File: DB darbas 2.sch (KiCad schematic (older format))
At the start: 20 parts, among them J1 XLR3_Ground, J3 XLR3_Ground, SW6 SW_DPST_x2, U1 Arduino_UNO_R2

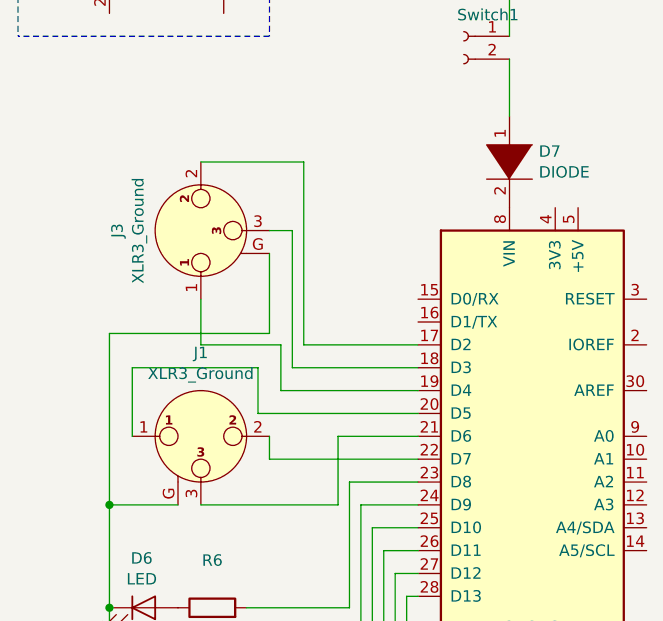
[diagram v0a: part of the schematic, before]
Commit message: DMX laidų testeris REV 1.2
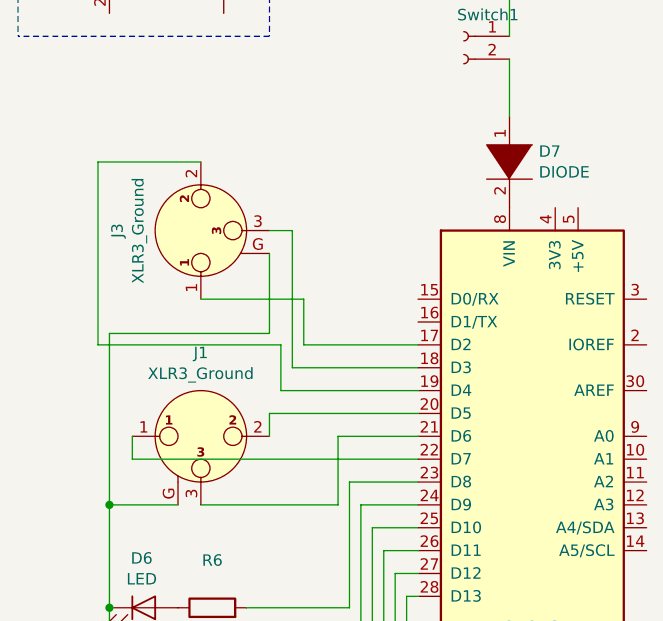
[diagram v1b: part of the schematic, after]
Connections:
- net at U1.17 (D2): now also J3.1; no longer J3.2
- net at U1.19 (D4): now also J3.2; no longer J3.1
- net at U1.20 (D5): now also J1.2; no longer J1.1
- net at U1.22 (D7): now also J1.1; no longer J1.2
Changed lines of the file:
@@
 Connection ~ 3700 5300
-Wire Wire Line
-	5050 2700 4350 2700
-Wire Wire Line
-	4350 2700 4350 2500
 Wire Wire Line
 	5050 2800 4700 2800
 Wire Wire Line
 	4700 2800 4700 3100
-Wire Wire Line
-	5050 2900 4400 2900
-Wire Wire Line
-	4400 2900 4400 2800
 Wire Wire Line
 	5650 4300 5550 4300
@@
 Wire Wire Line
 	5550 3900 5550 4300
-Wire Wire Line
-	4350 2500 3800 2500
-Wire Wire Line
-	3800 2500 3800 2800
 Wire Wire Line
 	4700 3100 4100 3100
@@
 	3700 3550 3700 3900
 Wire Wire Line
-	4100 1600 4550 1600
-Wire Wire Line
 	5550 5400 5550 5500
 Wire Wire Line
@@
 	3700 2350 3700 3100
 Connection ~ 3700 3100
-Wire Wire Line
-	4100 2200 4100 2400
-Wire Wire Line
-	4100 2400 4450 2400
 $Comp
 L pspice:DIODE D7
@@
 $EndComp
 Wire Wire Line
-	4550 1600 4550 2400
-Wire Wire Line
 	5450 1400 5450 1150
 Text Notes 4450 600  0    50   ~ 0
 Nemontuojama į PCB\n
+Wire Wire Line
+	3650 2400 3650 1600
+Wire Wire Line
+	3650 1600 4100 1600
+Wire Wire Line
+	3650 2400 4450 2400
+Wire Wire Line
+	4550 2400 4550 2200
+Wire Wire Line
+	4550 2200 4100 2200
+Wire Wire Line
+	5050 2700 4400 2700
+Wire Wire Line
+	4400 2700 4400 2800
+Wire Wire Line
+	5050 2900 3800 2900
+Wire Wire Line
+	3800 2900 3800 2800
 $EndSCHEMATC

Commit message: Ver1.3
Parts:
- removed Switch1: Conn_01x02_Female, Connector_PinHeader_2.54mm:PinHeader_1x02_P2.54mm_Horizontal, symbol Connector:Conn_01x02_Female
- removed VCC1: Connector, Connector_PinHeader_2.54mm:PinHeader_1x02_P2.54mm_Horizontal, symbol Connector:Conn_01x02_Female
- renumbered DC_9V1 to B1, J3 to J1, J1 to J2, SW6 to SW1
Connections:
- net GND: now also B1.2 (-)
- net at B1.1 (+): now also SW1.2 (B)
- net at SW1.1 (A): now also D7.1 (K)
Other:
- note removed: "Nemontuojama į PCB\n"
- moved on the sheet: B1, J1, J2, SW1A
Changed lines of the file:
@@
 U 1 1 5BE0B862
 P 3850 4600
-F 0 "D3" H 3841 4816 50  0000 C CNN
-F 1 "LED" H 3841 4725 50  0000 C CNN
+F 0 "D3" H 3850 5060 50  0000 C CNN
+F 1 "LED" H 3841 4725 50  0001 C CNN
 F 2 "LED_SMD:LED_0603_1608Metric_Pad1.05x0.95mm_HandSolder" H 3850 4600 50  0001 C CNN
 F 3 "~" H 3850 4600 50  0001 C CNN
@@
 U 1 1 5BE0B8D5
 P 4150 4600
-F 0 "R3" V 4357 4600 50  0000 C CNN
+F 0 "R3" V 4610 4600 50  0000 C CNN
 F 1 "300" V 4250 4550 50  0001 C CNN
 F 2 "Resistor_SMD:R_0603_1608Metric_Pad1.05x0.95mm_HandSolder" V 4080 4600 50  0001 C CNN
@@
 $EndComp
 $Comp
-L Device:Battery DC_9V1
+L Device:Battery B1
 U 1 1 5BE0F56A
-P 4200 750
-F 0 "DC_9V1" V 4445 750 50  0000 C CNN
-F 1 "Battery" V 4354 750 50  0001 C CNN
-F 2 "" V 4200 810 50  0001 C CNN
-F 3 "~" V 4200 810 50  0001 C CNN
-	1    4200 750
-	-1   0    0    1
-$EndComp
-Wire Wire Line
-	7100 800  7100 4300
+P 6750 1400
+F 0 "B1" V 6600 1400 50  0000 C CNN
+F 1 "Battery" V 6904 1400 50  0001 C CNN
+F 2 "" V 6750 1460 50  0001 C CNN
+F 3 "~" V 6750 1460 50  0001 C CNN
+	1    6750 1400
+	0    -1   -1   0
+$EndComp
 Wire Wire Line
 	7100 4300 5650 4300
@@
 	5650 4300 5650 3900
 $Comp
-L Switch:SW_DPST_x2 SW6
+L Switch:SW_DPST_x2 SW1
 U 1 1 5BE115DF
-P 3700 750
-F 0 "SW6" V 3746 662 50  0000 R CNN
-F 1 "SW_DPST_x2" V 3655 662 50  0001 R CNN
-F 2 "" H 3700 750 50  0001 C CNN
-F 3 "" H 3700 750 50  0001 C CNN
-	1    3700 750
-	0    1    1    0
+P 6000 1400
+F 0 "SW1" H 6100 1300 50  0000 R CNN
+F 1 "SW_DPST_x2" V 5955 1312 50  0001 R CNN
+F 2 "" H 6000 1400 50  0001 C CNN
+F 3 "" H 6000 1400 50  0001 C CNN
+	1    6000 1400
+	1    0    0    -1
 $EndComp
 $Comp
@@
 U 1 1 5BE11DF9
 P 3850 4250
-F 0 "D4" H 3841 4466 50  0000 C CNN
-F 1 "LED" H 3841 4375 50  0000 C CNN
+F 0 "D4" H 3850 4000 50  0000 C CNN
+F 1 "LED" H 3841 4375 50  0001 C CNN
 F 2 "LED_SMD:LED_0603_1608Metric_Pad1.05x0.95mm_HandSolder" H 3850 4250 50  0001 C CNN
 F 3 "~" H 3850 4250 50  0001 C CNN
@@
 U 1 1 5BE11DFF
 P 4150 4250
-F 0 "R4" V 4350 4250 50  0000 C CNN
+F 0 "R4" V 3900 4250 50  0000 C CNN
 F 1 "300" V 4250 4200 50  0001 C CNN
 F 2 "Resistor_SMD:R_0603_1608Metric_Pad1.05x0.95mm_HandSolder" V 4080 4250 50  0001 C CNN
@@
 U 1 1 5BE11FA5
 P 3850 5300
-F 0 "D1" H 3841 5516 50  0000 C CNN
-F 1 "LED" H 3841 5425 50  0000 C CNN
+F 0 "D1" H 3860 7150 50  0000 C CNN
+F 1 "LED" H 3841 5425 50  0001 C CNN
 F 2 "LED_SMD:LED_0603_1608Metric_Pad1.05x0.95mm_HandSolder" H 3850 5300 50  0001 C CNN
 F 3 "~" H 3850 5300 50  0001 C CNN
@@
 U 1 1 5BE11FAB
 P 4150 5300
-F 0 "R1" V 3950 5300 50  0000 C TNN
+F 0 "R1" V 2270 5300 50  0000 C TNN
 F 1 "300" V 4050 5350 50  0001 C CNN
 F 2 "Resistor_SMD:R_0603_1608Metric_Pad1.05x0.95mm_HandSolder" V 4080 5300 50  0001 C CNN
@@
 U 1 1 5BE11FB1
 P 3850 4950
-F 0 "D2" H 3841 5166 50  0000 C CNN
-F 1 "LED" H 3841 5075 50  0000 C CNN
+F 0 "D2" H 3850 6100 50  0000 C CNN
+F 1 "LED" H 3841 5075 50  0001 C CNN
 F 2 "LED_SMD:LED_0603_1608Metric_Pad1.05x0.95mm_HandSolder" H 3850 4950 50  0001 C CNN
 F 3 "~" H 3850 4950 50  0001 C CNN
@@
 U 1 1 5BE11FB7
 P 4150 4950
-F 0 "R2" V 4357 4950 50  0000 C CNN
+F 0 "R2" V 5300 4950 50  0000 C CNN
 F 1 "300" V 4250 4900 50  0001 C CNN
 F 2 "Resistor_SMD:R_0603_1608Metric_Pad1.05x0.95mm_HandSolder" V 4080 4950 50  0001 C CNN
@@
 U 1 1 5BE120E5
 P 3850 3900
-F 0 "D5" H 3841 4116 50  0000 C CNN
-F 1 "LED" H 3841 4025 50  0000 C CNN
+F 0 "D5" H 3840 2950 50  0000 C CNN
+F 1 "LED" H 3841 4025 50  0001 C CNN
 F 2 "LED_SMD:LED_0603_1608Metric_Pad1.05x0.95mm_HandSolder" H 3850 3900 50  0001 C CNN
 F 3 "~" H 3850 3900 50  0001 C CNN
@@
 U 1 1 5BE120EB
 P 4150 3900
-F 0 "R5" V 4357 3900 50  0000 C CNN
+F 0 "R5" V 3200 3910 50  0000 C CNN
 F 1 "300" V 4250 3850 50  0001 C CNN
 F 2 "Resistor_SMD:R_0603_1608Metric_Pad1.05x0.95mm_HandSolder" V 4080 3900 50  0001 C CNN
@@
 U 1 1 5BE120F1
 P 3850 3550
-F 0 "D6" H 3841 3766 50  0000 C CNN
-F 1 "LED" H 3841 3675 50  0000 C CNN
+F 0 "D6" H 3850 1900 50  0000 C CNN
+F 1 "LED" H 3841 3675 50  0001 C CNN
 F 2 "LED_SMD:LED_0603_1608Metric_Pad1.05x0.95mm_HandSolder" H 3850 3550 50  0001 C CNN
 F 3 "~" H 3850 3550 50  0001 C CNN
@@
 U 1 1 5BE120F7
 P 4150 3550
-F 0 "R6" V 4357 3550 50  0000 C CNN
+F 0 "R6" V 2500 3570 50  0000 C CNN
 F 1 "300" V 4250 3500 50  0001 C CNN
 F 2 "Resistor_SMD:R_0603_1608Metric_Pad1.05x0.95mm_HandSolder" V 4080 3550 50  0001 C CNN
@@
 	0    -1   -1   0
 $EndComp
-$Comp
-L Connector:Conn_01x02_Female VCC1
-U 1 1 5BE12452
-P 5600 600
-F 0 "VCC1" V 5540 412 50  0000 R CNN
-F 1 "Connector" V 5449 412 50  0001 R CNN
-F 2 "Connector_PinHeader_2.54mm:PinHeader_1x02_P2.54mm_Horizontal" H 5600 600 50  0001 C CNN
-F 3 "~" H 5600 600 50  0001 C CNN
-	1    5600 600
-	0    -1   -1   0
-$EndComp
-$Comp
-L Connector:Conn_01x02_Female Switch1
-U 1 1 5BE124E0
-P 5250 1050
-F 0 "Switch1" H 5144 1143 50  0000 C CNN
-F 1 "Conn_01x02_Female" H 5144 1144 50  0001 C CNN
-F 2 "Connector_PinHeader_2.54mm:PinHeader_1x02_P2.54mm_Horizontal" H 5250 1050 50  0001 C CNN
-F 3 "~" H 5250 1050 50  0001 C CNN
-	1    5250 1050
-	-1   0    0    -1
-$EndComp
-Wire Wire Line
-	5450 800  5450 1050
-Wire Wire Line
-	5450 800  5600 800
-Wire Wire Line
-	5700 800  6300 800
 Wire Wire Line
 	3700 5300 3700 4950
@@
 	4750 3000 5050 3000
 Wire Wire Line
-	4450 2400 4450 2600
-Wire Wire Line
 	4450 2600 5050 2600
-Wire Wire Line
-	4500 1900 4500 2500
-Wire Wire Line
-	4500 2500 5050 2500
-Wire Wire Line
-	4550 2400 5050 2400
 Wire Wire Line
 	5550 5400 3700 5400
@@
 	3700 5400 3700 5300
 Connection ~ 3700 5300
-Wire Wire Line
-	5050 2800 4700 2800
-Wire Wire Line
-	4700 2800 4700 3100
 Wire Wire Line
 	5650 4300 5550 4300
@@
 Wire Wire Line
 	5550 4300 5550 5400
-Wire Notes Line
-	3300 500  4400 500
-Wire Notes Line
-	4400 500  4400 1050
-Wire Notes Line
-	4400 1050 3300 1050
-Wire Notes Line
-	3300 500  3300 1050
 Wire Wire Line
 	5550 3900 5550 4300
-Wire Wire Line
-	4700 3100 4100 3100
-Text Label 6000 800  0    50   ~ 0
-vcc
 $Comp
 L power:GND #PWR0101
@@
 Connection ~ 5550 5400
 $Comp
-L power:VCC #PWR0102
-U 1 1 5BFC947E
-P 6300 800
-F 0 "#PWR0102" H 6300 650 50  0001 C CNN
-F 1 "VCC" H 6317 973 50  0000 C CNN
-F 2 "" H 6300 800 50  0001 C CNN
-F 3 "" H 6300 800 50  0001 C CNN
-	1    6300 800
-	1    0    0    -1
-$EndComp
-Connection ~ 6300 800
-Wire Wire Line
-	6300 800  7100 800
-$Comp
-L Connector:XLR3_Ground J3
+L Connector:XLR3_Ground J1
 U 1 1 5BFCA7B8
-P 4100 1900
-F 0 "J3" H 4100 2265 50  0000 C CNN
-F 1 "XLR3_Ground" H 4100 2174 50  0000 C CNN
-F 2 "XLR_mano:XLR_footprint" H 4100 1900 50  0001 C CNN
-F 3 " ~" H 4100 1900 50  0001 C CNN
-	1    4100 1900
-	0    -1   -1   0
-$EndComp
-$Comp
-L Connector:XLR3_Ground J1
-U 1 1 5BFD097B
-P 4100 2800
-F 0 "J1" H 4100 3165 50  0000 C CNN
-F 1 "XLR3_Ground" H 4100 3074 50  0000 C CNN
-F 2 "XLR_mano:XLR_footprint" H 4100 2800 50  0001 C CNN
-F 3 " ~" H 4100 2800 50  0001 C CNN
-	1    4100 2800
-	1    0    0    -1
-$EndComp
-Wire Wire Line
-	4000 3100 3700 3100
-Wire Wire Line
-	3700 3100 3700 3550
+P 4100 2000
+F 0 "J1" V 4100 2250 50  0000 C CNN
+F 1 "XLR3_Ground" H 4100 2274 50  0001 C CNN
+F 2 "XLR_mano:XLR_footprint" H 4100 2000 50  0001 C CNN
+F 3 " ~" H 4100 2000 50  0001 C CNN
+	1    4100 2000
+	0    1    1    0
+$EndComp
 Connection ~ 3700 3550
 Wire Wire Line
@@
 Wire Wire Line
 	5550 5400 5550 5500
-Wire Wire Line
-	4400 1900 4500 1900
-Wire Wire Line
-	4400 2000 4400 2350
-Wire Wire Line
-	4400 2350 3700 2350
-Wire Wire Line
-	3700 2350 3700 3100
-Connection ~ 3700 3100
 $Comp
 L pspice:DIODE D7
 U 1 1 5BFC56E1
 P 5450 1600
-F 0 "D7" V 5404 1728 50  0000 L CNN
-F 1 "DIODE" V 5495 1728 50  0000 L CNN
+F 0 "D7" V 5450 1750 50  0000 L CNN
+F 1 "DIODE" V 5495 1728 50  0001 L CNN
 F 2 "Diode_SMD:D_0603_1608Metric_Pad1.05x0.95mm_HandSolder" H 5450 1600 50  0001 C CNN
 F 3 "~" H 5450 1600 50  0001 C CNN
@@
 $EndComp
 Wire Wire Line
-	5450 1400 5450 1150
-Text Notes 4450 600  0    50   ~ 0
-Nemontuojama į PCB\n
-Wire Wire Line
-	3650 2400 3650 1600
-Wire Wire Line
-	3650 1600 4100 1600
-Wire Wire Line
-	3650 2400 4450 2400
-Wire Wire Line
-	4550 2400 4550 2200
-Wire Wire Line
-	4550 2200 4100 2200
-Wire Wire Line
-	5050 2700 4400 2700
-Wire Wire Line
-	4400 2700 4400 2800
-Wire Wire Line
-	5050 2900 3800 2900
-Wire Wire Line
-	3800 2900 3800 2800
+	5450 1400 5800 1400
+Wire Wire Line
+	6200 1400 6550 1400
+Wire Wire Line
+	7100 4300 7100 1400
+Wire Wire Line
+	7100 1400 6950 1400
+$Comp
+L Connector:XLR3_Ground J2
+U 1 1 5BFD097B
+P 4100 2800
+F 0 "J2" V 4100 3050 50  0000 C CNN
+F 1 "XLR3_Ground" H 4100 3074 50  0001 C CNN
+F 2 "XLR_mano:XLR_footprint" H 4100 2800 50  0001 C CNN
+F 3 " ~" H 4100 2800 50  0001 C CNN
+	1    4100 2800
+	0    1    -1   0
+$EndComp
+Wire Wire Line
+	4300 2900 4300 3100
+Wire Wire Line
+	4300 3100 4100 3100
+Wire Wire Line
+	4300 2900 5050 2900
+Wire Wire Line
+	5050 2700 4350 2700
+Wire Wire Line
+	4350 2700 4350 2500
+Wire Wire Line
+	4350 2500 4100 2500
+Wire Wire Line
+	5050 2800 4400 2800
+Wire Wire Line
+	4400 2800 4400 2450
+Wire Wire Line
+	3800 2450 3800 2800
+Wire Wire Line
+	3800 2900 3700 2900
+Connection ~ 3700 2900
+Wire Wire Line
+	3700 2900 3700 3550
+Wire Wire Line
+	3800 2450 4400 2450
+Wire Wire Line
+	5050 2400 4900 2400
+Wire Wire Line
+	4900 2400 4900 1700
+Wire Wire Line
+	4900 1700 4100 1700
+Wire Wire Line
+	4450 2600 4450 2400
+Wire Wire Line
+	4450 2400 4100 2400
+Wire Wire Line
+	4100 2400 4100 2300
+Wire Wire Line
+	5050 2500 4500 2500
+Wire Wire Line
+	4500 2500 4500 2350
+Wire Wire Line
+	4500 2350 3800 2350
+Wire Wire Line
+	3800 2350 3800 2000
+Wire Wire Line
+	3700 1900 3800 1900
+Wire Wire Line
+	3700 1900 3700 2900
 $EndSCHEMATC
